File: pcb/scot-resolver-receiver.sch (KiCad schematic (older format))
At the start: 12 parts, among them IC3 AD8692ARMZ

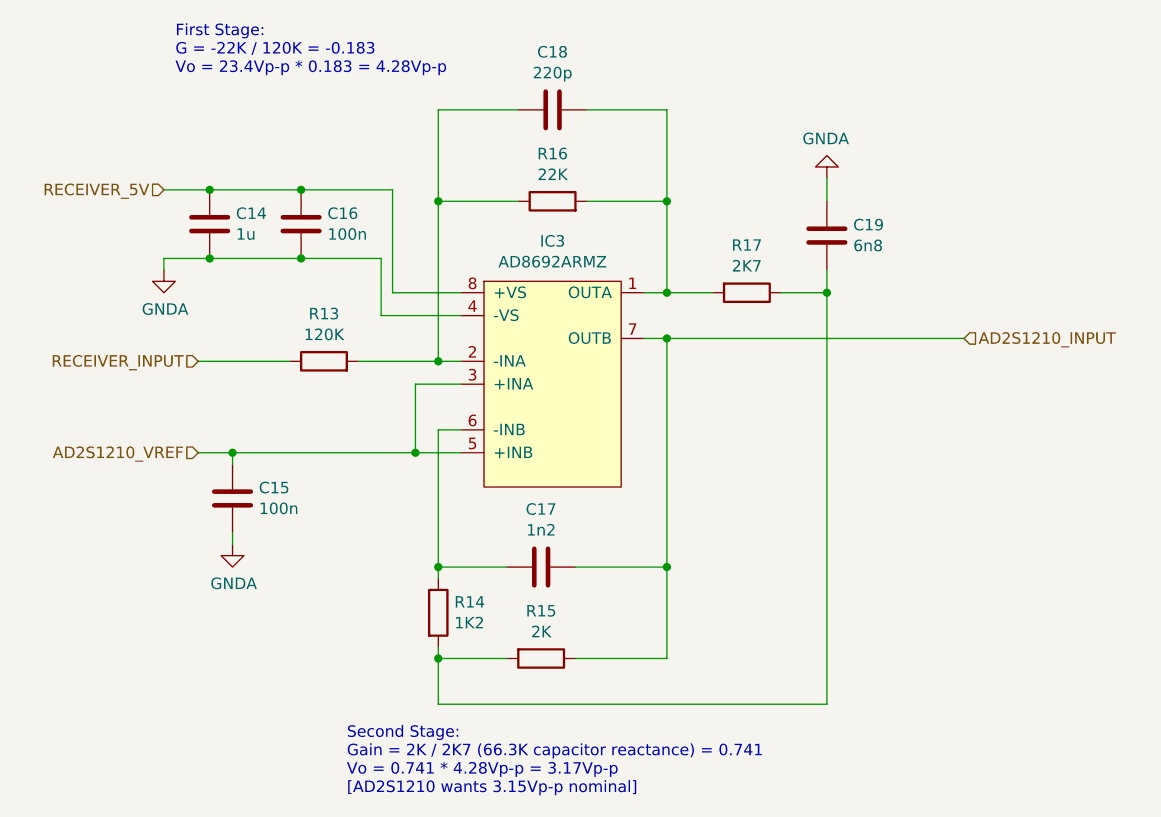
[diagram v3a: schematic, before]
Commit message: pcb: Add 10u to VREF, all 0402->0603
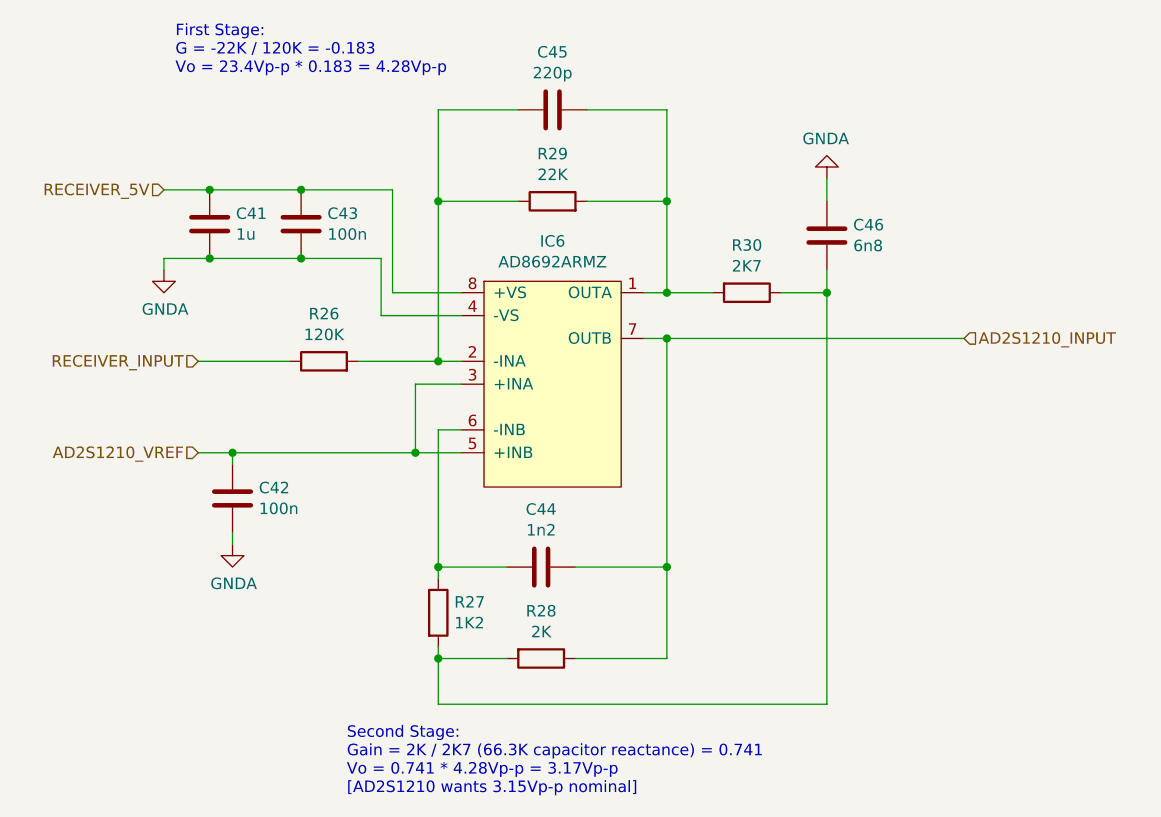
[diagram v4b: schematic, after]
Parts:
- C15, C16, C17, C18, C19: footprint Capacitor_SMD:C_0402_1005Metric -> Capacitor_SMD:C_0603_1608Metric_Pad1.05x0.95mm_HandSolder
- R13, R14, R15, R16, R17: footprint Resistor_SMD:R_0402_1005Metric -> Resistor_SMD:R_0603_1608Metric_Pad1.05x0.95mm_HandSolder
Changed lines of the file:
@@
 $Descr A4 11693 8268
 encoding utf-8
-Sheet 3 7
+Sheet 5 7
 Title ""
 Date ""
@@
 AR Path="/5E46F57D/5E2564F7" Ref="IC6"  Part="1"
 AR Path="/5E46F583/5E2564F7" Ref="IC7"  Part="1"
-F 0 "IC3" H 5100 3925 50  0000 C CNN
+F 0 "IC6" H 5100 3925 50  0000 C CNN
 F 1 "AD8692ARMZ" H 5100 3834 50  0000 C CNN
 F 2 "agg:MSOP-8" H 4800 2700 50  0001 L CNN
@@
 AR Path="/5E46F57D/5E256D1D" Ref="R30"  Part="1"
 AR Path="/5E46F583/5E256D1D" Ref="R35"  Part="1"
-F 0 "R17" V 5743 2900 50  0000 C CNN
+F 0 "R30" V 5743 2900 50  0000 C CNN
 F 1 "2K7" V 5834 2900 50  0000 C CNN
-F 2 "Resistor_SMD:R_0402_1005Metric" V 5880 2900 50  0001 C CNN
+F 2 "Resistor_SMD:R_0603_1608Metric_Pad1.05x0.95mm_HandSolder" V 5880 2900 50  0001 C CNN
 F 3 "~" H 5950 2900 50  0001 C CNN
 	1    5950 2900
@@
 AR Path="/5E46F57D/5E257610" Ref="C46"  Part="1"
 AR Path="/5E46F583/5E257610" Ref="C52"  Part="1"
-F 0 "C19" H 6185 2604 50  0000 R CNN
+F 0 "C46" H 6185 2604 50  0000 R CNN
 F 1 "6n8" H 6185 2695 50  0000 R CNN
-F 2 "Capacitor_SMD:C_0402_1005Metric" H 6338 2500 50  0001 C CNN
+F 2 "Capacitor_SMD:C_0603_1608Metric_Pad1.05x0.95mm_HandSolder" H 6338 2500 50  0001 C CNN
 F 3 "~" H 6300 2650 50  0001 C CNN
 	1    6300 2650
@@
 AR Path="/5E46F57D/5E258A95" Ref="R28"  Part="1"
 AR Path="/5E46F583/5E258A95" Ref="R33"  Part="1"
-F 0 "R15" V 4843 4500 50  0000 C CNN
+F 0 "R28" V 4843 4500 50  0000 C CNN
 F 1 "2K" V 4934 4500 50  0000 C CNN
-F 2 "Resistor_SMD:R_0402_1005Metric" V 4980 4500 50  0001 C CNN
+F 2 "Resistor_SMD:R_0603_1608Metric_Pad1.05x0.95mm_HandSolder" V 4980 4500 50  0001 C CNN
 F 3 "~" H 5050 4500 50  0001 C CNN
 	1    5050 4500
@@
 AR Path="/5E46F57D/5E258E42" Ref="C44"  Part="1"
 AR Path="/5E46F583/5E258E42" Ref="C50"  Part="1"
-F 0 "C17" V 5302 4100 50  0000 C CNN
+F 0 "C44" V 5302 4100 50  0000 C CNN
 F 1 "1n2" V 5211 4100 50  0000 C CNN
-F 2 "Capacitor_SMD:C_0402_1005Metric" H 5088 3950 50  0001 C CNN
+F 2 "Capacitor_SMD:C_0603_1608Metric_Pad1.05x0.95mm_HandSolder" H 5088 3950 50  0001 C CNN
 F 3 "~" H 5050 4100 50  0001 C CNN
 	1    5050 4100
@@
 AR Path="/5E46F57D/5E25A0BD" Ref="R27"  Part="1"
 AR Path="/5E46F583/5E25A0BD" Ref="R32"  Part="1"
-F 0 "R14" H 4670 4346 50  0000 L CNN
+F 0 "R27" H 4670 4346 50  0000 L CNN
 F 1 "1K2" H 4670 4255 50  0000 L CNN
-F 2 "Resistor_SMD:R_0402_1005Metric" V 4530 4300 50  0001 C CNN
+F 2 "Resistor_SMD:R_0603_1608Metric_Pad1.05x0.95mm_HandSolder" V 4530 4300 50  0001 C CNN
 F 3 "~" H 4600 4300 50  0001 C CNN
 	1    4600 4300
@@
 AR Path="/5E46F57D/5E25CCF3" Ref="R29"  Part="1"
 AR Path="/5E46F583/5E25CCF3" Ref="R34"  Part="1"
-F 0 "R16" V 5307 2500 50  0000 C CNN
+F 0 "R29" V 5307 2500 50  0000 C CNN
 F 1 "22K" V 5216 2500 50  0000 C CNN
-F 2 "Resistor_SMD:R_0402_1005Metric" V 5030 2500 50  0001 C CNN
+F 2 "Resistor_SMD:R_0603_1608Metric_Pad1.05x0.95mm_HandSolder" V 5030 2500 50  0001 C CNN
 F 3 "~" H 5100 2500 50  0001 C CNN
 	1    5100 2500
@@
 AR Path="/5E46F57D/5E25ECB5" Ref="C45"  Part="1"
 AR Path="/5E46F583/5E25ECB5" Ref="C51"  Part="1"
-F 0 "C18" V 5352 2100 50  0000 C CNN
+F 0 "C45" V 5352 2100 50  0000 C CNN
 F 1 "220p" V 5261 2100 50  0000 C CNN
-F 2 "Capacitor_SMD:C_0402_1005Metric" H 5138 1950 50  0001 C CNN
+F 2 "Capacitor_SMD:C_0603_1608Metric_Pad1.05x0.95mm_HandSolder" H 5138 1950 50  0001 C CNN
 F 3 "~" H 5100 2100 50  0001 C CNN
 	1    5100 2100
@@
 AR Path="/5E46F57D/5E25FD02" Ref="R26"  Part="1"
 AR Path="/5E46F583/5E25FD02" Ref="R31"  Part="1"
-F 0 "R13" V 4307 3200 50  0000 C CNN
+F 0 "R26" V 4307 3200 50  0000 C CNN
 F 1 "120K" V 4216 3200 50  0000 C CNN
-F 2 "Resistor_SMD:R_0402_1005Metric" V 4030 3200 50  0001 C CNN
+F 2 "Resistor_SMD:R_0603_1608Metric_Pad1.05x0.95mm_HandSolder" V 4030 3200 50  0001 C CNN
 F 3 "~" H 4100 3200 50  0001 C CNN
 	1    4100 3200
@@
 AR Path="/5E46F57D/5E281514" Ref="C43"  Part="1"
 AR Path="/5E46F583/5E281514" Ref="C49"  Part="1"
-F 0 "C16" H 3885 2554 50  0000 R CNN
+F 0 "C43" H 3885 2554 50  0000 R CNN
 F 1 "100n" H 3885 2645 50  0000 R CNN
-F 2 "Capacitor_SMD:C_0402_1005Metric" H 4038 2450 50  0001 C CNN
+F 2 "Capacitor_SMD:C_0603_1608Metric_Pad1.05x0.95mm_HandSolder" H 4038 2450 50  0001 C CNN
 F 3 "~" H 4000 2600 50  0001 C CNN
 	1    4000 2600
@@
 AR Path="/5E46F57D/5E297D03" Ref="C42"  Part="1"
 AR Path="/5E46F583/5E297D03" Ref="C48"  Part="1"
-F 0 "C15" H 3585 3754 50  0000 R CNN
+F 0 "C42" H 3585 3754 50  0000 R CNN
 F 1 "100n" H 3585 3845 50  0000 R CNN
-F 2 "Capacitor_SMD:C_0402_1005Metric" H 3738 3650 50  0001 C CNN
+F 2 "Capacitor_SMD:C_0603_1608Metric_Pad1.05x0.95mm_HandSolder" H 3738 3650 50  0001 C CNN
 F 3 "~" H 3700 3800 50  0001 C CNN
 	1    3700 3800
@@
 AR Path="/5E46F57D/5E29C4B1" Ref="C41"  Part="1"
 AR Path="/5E46F583/5E29C4B1" Ref="C47"  Part="1"
-F 0 "C14" H 3485 2554 50  0000 R CNN
+F 0 "C41" H 3485 2554 50  0000 R CNN
 F 1 "1u" H 3485 2645 50  0000 R CNN
 F 2 "Capacitor_SMD:C_0603_1608Metric_Pad1.05x0.95mm_HandSolder" H 3638 2450 50  0001 C CNN
@@
 AR Path="/5E46F57D/5E28F597" Ref="#PWR0130"  Part="1"
 AR Path="/5E46F583/5E28F597" Ref="#PWR0133"  Part="1"
-F 0 "#PWR0110" H 3400 2550 50  0001 C CNN
+F 0 "#PWR0130" H 3400 2550 50  0001 C CNN
 F 1 "GNDA" H 3405 2627 50  0000 C CNN
 F 2 "" H 3400 2800 50  0001 C CNN
@@
 AR Path="/5E46F57D/5E28F9AD" Ref="#PWR0131"  Part="1"
 AR Path="/5E46F583/5E28F9AD" Ref="#PWR0134"  Part="1"
-F 0 "#PWR0111" H 3700 3750 50  0001 C CNN
+F 0 "#PWR0131" H 3700 3750 50  0001 C CNN
 F 1 "GNDA" H 3705 3827 50  0000 C CNN
 F 2 "" H 3700 4000 50  0001 C CNN
@@
 AR Path="/5E46F57D/5E28FD4C" Ref="#PWR0132"  Part="1"
 AR Path="/5E46F583/5E28FD4C" Ref="#PWR0135"  Part="1"
-F 0 "#PWR0112" H 6300 2150 50  0001 C CNN
+F 0 "#PWR0132" H 6300 2150 50  0001 C CNN
 F 1 "GNDA" H 6305 2227 50  0000 C CNN
 F 2 "" H 6300 2400 50  0001 C CNN

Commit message: pcb: Add v2 BOM, fix some component values.
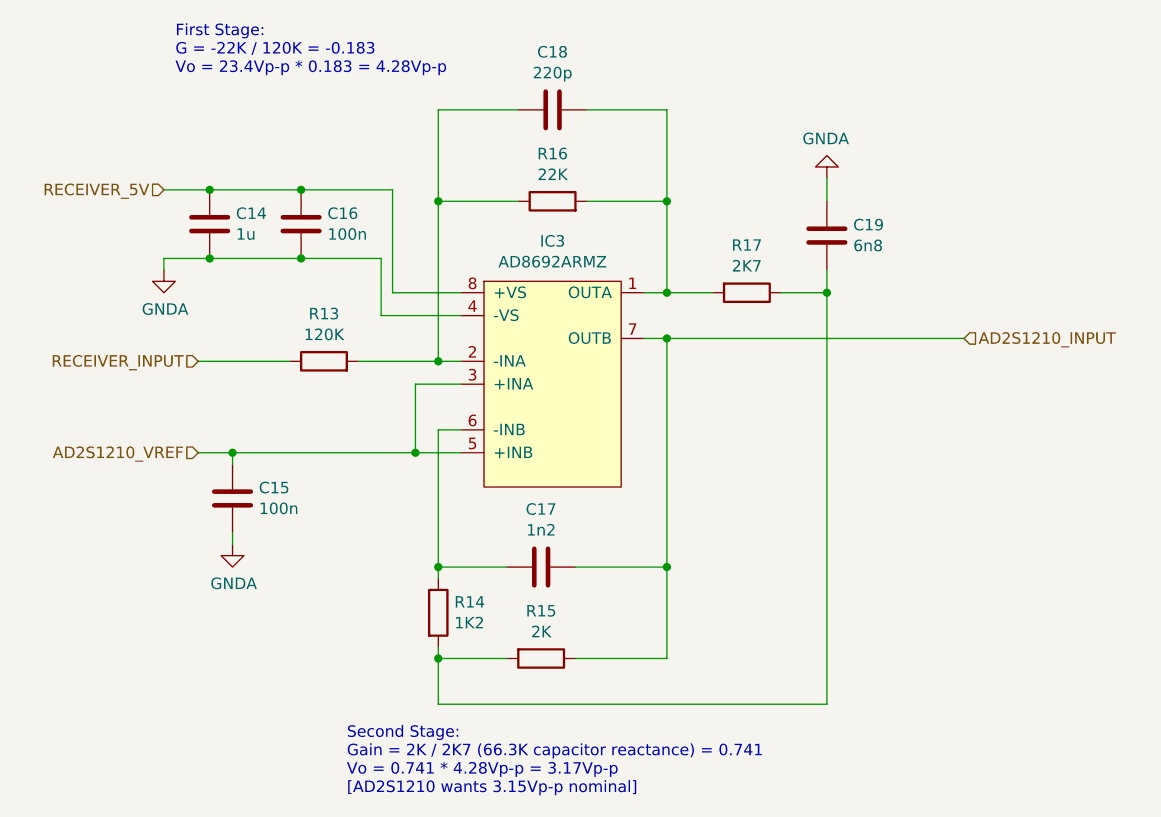
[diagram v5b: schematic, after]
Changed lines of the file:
@@
 $Descr A4 11693 8268
 encoding utf-8
-Sheet 5 7
+Sheet 2 7
 Title ""
 Date ""
@@
 AR Path="/5E46F57D/5E2564F7" Ref="IC6"  Part="1"
 AR Path="/5E46F583/5E2564F7" Ref="IC7"  Part="1"
-F 0 "IC6" H 5100 3925 50  0000 C CNN
+F 0 "IC3" H 5100 3925 50  0000 C CNN
 F 1 "AD8692ARMZ" H 5100 3834 50  0000 C CNN
 F 2 "agg:MSOP-8" H 4800 2700 50  0001 L CNN
@@
 AR Path="/5E46F57D/5E256D1D" Ref="R30"  Part="1"
 AR Path="/5E46F583/5E256D1D" Ref="R35"  Part="1"
-F 0 "R30" V 5743 2900 50  0000 C CNN
+F 0 "R17" V 5743 2900 50  0000 C CNN
 F 1 "2K7" V 5834 2900 50  0000 C CNN
 F 2 "Resistor_SMD:R_0603_1608Metric_Pad1.05x0.95mm_HandSolder" V 5880 2900 50  0001 C CNN
@@
 AR Path="/5E46F57D/5E257610" Ref="C46"  Part="1"
 AR Path="/5E46F583/5E257610" Ref="C52"  Part="1"
-F 0 "C46" H 6185 2604 50  0000 R CNN
+F 0 "C19" H 6185 2604 50  0000 R CNN
 F 1 "6n8" H 6185 2695 50  0000 R CNN
 F 2 "Capacitor_SMD:C_0603_1608Metric_Pad1.05x0.95mm_HandSolder" H 6338 2500 50  0001 C CNN
@@
 AR Path="/5E46F57D/5E258A95" Ref="R28"  Part="1"
 AR Path="/5E46F583/5E258A95" Ref="R33"  Part="1"
-F 0 "R28" V 4843 4500 50  0000 C CNN
+F 0 "R15" V 4843 4500 50  0000 C CNN
 F 1 "2K" V 4934 4500 50  0000 C CNN
 F 2 "Resistor_SMD:R_0603_1608Metric_Pad1.05x0.95mm_HandSolder" V 4980 4500 50  0001 C CNN
@@
 AR Path="/5E46F57D/5E258E42" Ref="C44"  Part="1"
 AR Path="/5E46F583/5E258E42" Ref="C50"  Part="1"
-F 0 "C44" V 5302 4100 50  0000 C CNN
+F 0 "C17" V 5302 4100 50  0000 C CNN
 F 1 "1n2" V 5211 4100 50  0000 C CNN
 F 2 "Capacitor_SMD:C_0603_1608Metric_Pad1.05x0.95mm_HandSolder" H 5088 3950 50  0001 C CNN
@@
 AR Path="/5E46F57D/5E25A0BD" Ref="R27"  Part="1"
 AR Path="/5E46F583/5E25A0BD" Ref="R32"  Part="1"
-F 0 "R27" H 4670 4346 50  0000 L CNN
+F 0 "R14" H 4670 4346 50  0000 L CNN
 F 1 "1K2" H 4670 4255 50  0000 L CNN
 F 2 "Resistor_SMD:R_0603_1608Metric_Pad1.05x0.95mm_HandSolder" V 4530 4300 50  0001 C CNN
@@
 AR Path="/5E46F57D/5E25CCF3" Ref="R29"  Part="1"
 AR Path="/5E46F583/5E25CCF3" Ref="R34"  Part="1"
-F 0 "R29" V 5307 2500 50  0000 C CNN
+F 0 "R16" V 5307 2500 50  0000 C CNN
 F 1 "22K" V 5216 2500 50  0000 C CNN
 F 2 "Resistor_SMD:R_0603_1608Metric_Pad1.05x0.95mm_HandSolder" V 5030 2500 50  0001 C CNN
@@
 AR Path="/5E46F57D/5E25ECB5" Ref="C45"  Part="1"
 AR Path="/5E46F583/5E25ECB5" Ref="C51"  Part="1"
-F 0 "C45" V 5352 2100 50  0000 C CNN
+F 0 "C18" V 5352 2100 50  0000 C CNN
 F 1 "220p" V 5261 2100 50  0000 C CNN
 F 2 "Capacitor_SMD:C_0603_1608Metric_Pad1.05x0.95mm_HandSolder" H 5138 1950 50  0001 C CNN
@@
 AR Path="/5E46F57D/5E25FD02" Ref="R26"  Part="1"
 AR Path="/5E46F583/5E25FD02" Ref="R31"  Part="1"
-F 0 "R26" V 4307 3200 50  0000 C CNN
+F 0 "R13" V 4307 3200 50  0000 C CNN
 F 1 "120K" V 4216 3200 50  0000 C CNN
 F 2 "Resistor_SMD:R_0603_1608Metric_Pad1.05x0.95mm_HandSolder" V 4030 3200 50  0001 C CNN
@@
 AR Path="/5E46F57D/5E281514" Ref="C43"  Part="1"
 AR Path="/5E46F583/5E281514" Ref="C49"  Part="1"
-F 0 "C43" H 3885 2554 50  0000 R CNN
+F 0 "C16" H 3885 2554 50  0000 R CNN
 F 1 "100n" H 3885 2645 50  0000 R CNN
 F 2 "Capacitor_SMD:C_0603_1608Metric_Pad1.05x0.95mm_HandSolder" H 4038 2450 50  0001 C CNN
@@
 AR Path="/5E46F57D/5E297D03" Ref="C42"  Part="1"
 AR Path="/5E46F583/5E297D03" Ref="C48"  Part="1"
-F 0 "C42" H 3585 3754 50  0000 R CNN
+F 0 "C15" H 3585 3754 50  0000 R CNN
 F 1 "100n" H 3585 3845 50  0000 R CNN
 F 2 "Capacitor_SMD:C_0603_1608Metric_Pad1.05x0.95mm_HandSolder" H 3738 3650 50  0001 C CNN
@@
 AR Path="/5E46F57D/5E29C4B1" Ref="C41"  Part="1"
 AR Path="/5E46F583/5E29C4B1" Ref="C47"  Part="1"
-F 0 "C41" H 3485 2554 50  0000 R CNN
+F 0 "C14" H 3485 2554 50  0000 R CNN
 F 1 "1u" H 3485 2645 50  0000 R CNN
 F 2 "Capacitor_SMD:C_0603_1608Metric_Pad1.05x0.95mm_HandSolder" H 3638 2450 50  0001 C CNN
@@
 AR Path="/5E46F57D/5E28F597" Ref="#PWR0130"  Part="1"
 AR Path="/5E46F583/5E28F597" Ref="#PWR0133"  Part="1"
-F 0 "#PWR0130" H 3400 2550 50  0001 C CNN
+F 0 "#PWR0110" H 3400 2550 50  0001 C CNN
 F 1 "GNDA" H 3405 2627 50  0000 C CNN
 F 2 "" H 3400 2800 50  0001 C CNN
@@
 AR Path="/5E46F57D/5E28F9AD" Ref="#PWR0131"  Part="1"
 AR Path="/5E46F583/5E28F9AD" Ref="#PWR0134"  Part="1"
-F 0 "#PWR0131" H 3700 3750 50  0001 C CNN
+F 0 "#PWR0111" H 3700 3750 50  0001 C CNN
 F 1 "GNDA" H 3705 3827 50  0000 C CNN
 F 2 "" H 3700 4000 50  0001 C CNN
@@
 AR Path="/5E46F57D/5E28FD4C" Ref="#PWR0132"  Part="1"
 AR Path="/5E46F583/5E28FD4C" Ref="#PWR0135"  Part="1"
-F 0 "#PWR0132" H 6300 2150 50  0001 C CNN
+F 0 "#PWR0112" H 6300 2150 50  0001 C CNN
 F 1 "GNDA" H 6305 2227 50  0000 C CNN
 F 2 "" H 6300 2400 50  0001 C CNN
